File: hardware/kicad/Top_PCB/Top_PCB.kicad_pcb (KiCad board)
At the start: 2 copper layers, 30.8 x 26.8 mm, 3 parts, among them J1 XT30PW-M

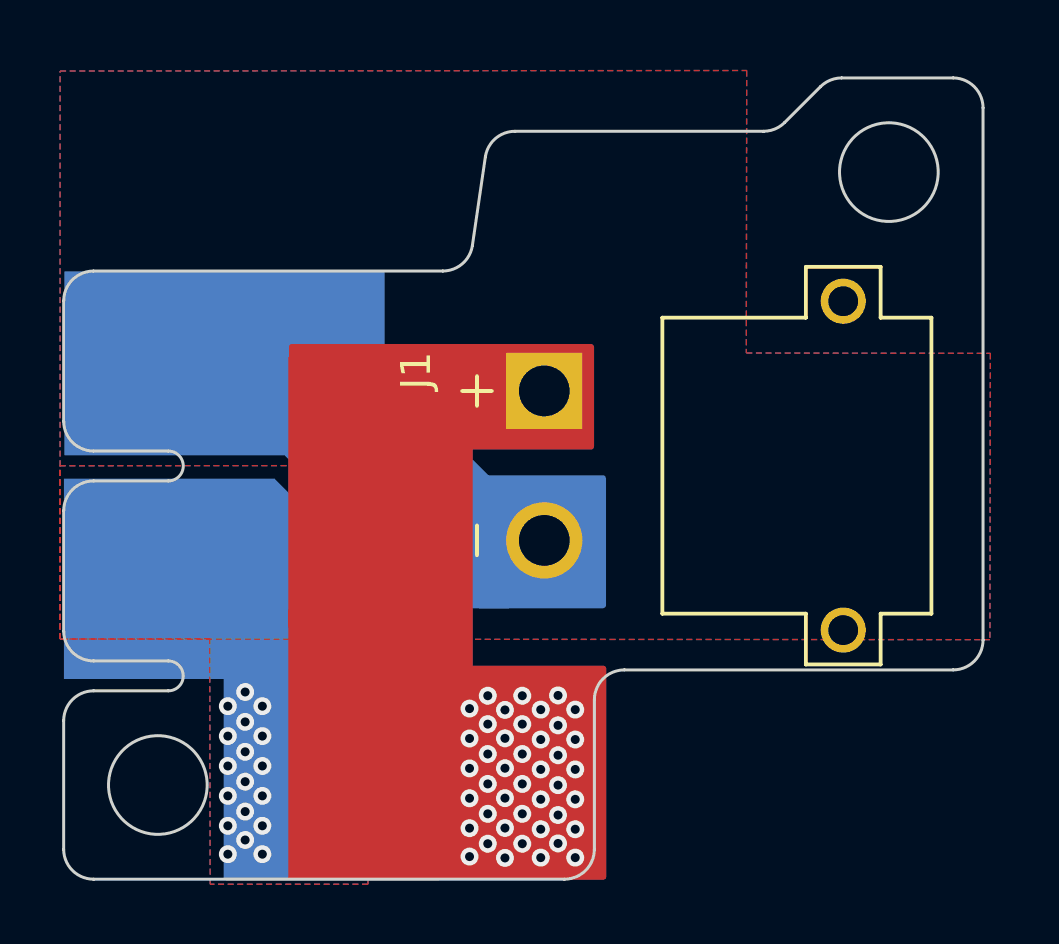
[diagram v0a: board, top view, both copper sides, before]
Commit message: Did some top board work (added regulator), added vias and refined geometry a bit
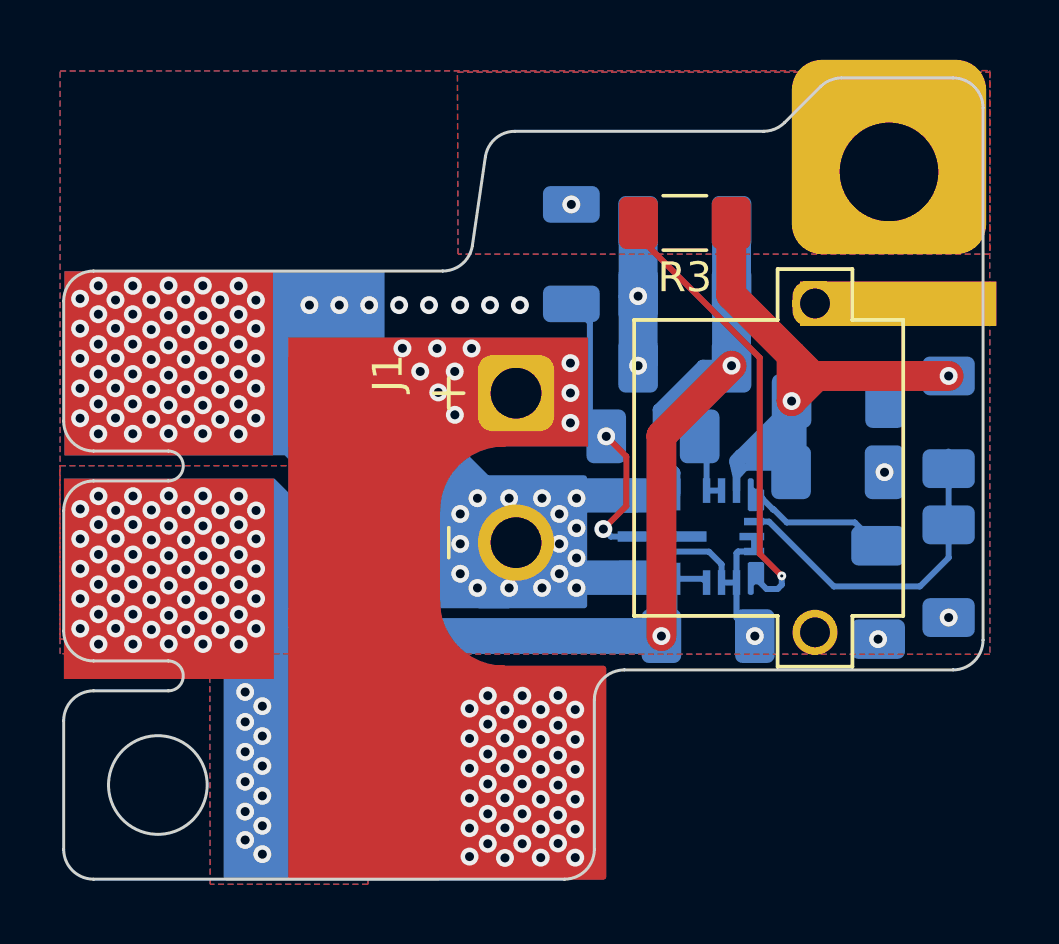
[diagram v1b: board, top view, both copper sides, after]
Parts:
- added C2: 10uF, Capacitor_SMD:C_1206_3216Metric_Pad1.33x1.80mm_HandSolder, B.Cu at (131.5, 89.3)
- added C3: 10uF, Capacitor_SMD:C_1206_3216Metric_Pad1.33x1.80mm_HandSolder, B.Cu at (131.5, 91.7)
- added C4: 1uF, Capacitor_SMD:C_1206_3216Metric_Pad1.33x1.80mm_HandSolder, B.Cu at (131.5, 94.1)
- added C5: 1uF, Capacitor_SMD:C_1206_3216Metric_Pad1.33x1.80mm_HandSolder, B.Cu at (132.3, 103.1)
- added C6: 100nF, Capacitor_SMD:C_1206_3216Metric_Pad1.33x1.80mm_HandSolder, B.Cu at (130.4, 96.4)
- added C7: 22uF, Capacitor_SMD:C_1206_3216Metric_Pad1.33x1.80mm_HandSolder, B.Cu at (136.6, 95.2)
- added C8: 1uF, Capacitor_SMD:C_1206_3216Metric_Pad1.33x1.80mm_HandSolder, B.Cu at (138.0, 101.6)
- added C9: 100nF, Capacitor_SMD:C_1206_3216Metric_Pad1.33x1.80mm_HandSolder, B.Cu at (136.6, 97.6)
- added L1: 640nH, Inductor_SMD:L_1206_3216Metric_Pad1.22x1.90mm_HandSolder, B.Cu at (127.7, 90.3)
- added R1: 100k, PCB-V2-Footprints:R_1206_3216Metric_Pad1.30x1.75mm_HandSolder, B.Cu at (140.3, 96.0)
- added R2: 14.3k, PCB-V2-Footprints:R_1206_3216Metric_Pad1.30x1.75mm_HandSolder, B.Cu at (140.3, 100.9)
- added R3: 100k, PCB-V2-Footprints:R_1206_3216Metric_Pad1.30x1.75mm_HandSolder, F.Cu at (131.5, 89.3)
- added U1: LM61495RPHR, LM61480Q3RPHRQ1:RPH0016A, B.Cu at (131.7, 99.8)
- added VCC_8V1: ~, Pads:VCC_Standalone, B.Cu at (138.3, 87.6)
- moved J1 0.95 mm to (135.8, 97.5)
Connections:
- J1 pad S1: (no net) -> GND
- J1 pad S2: (no net) -> GND
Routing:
- net VCC_4S: track 0.00 -> 36.8 mm, vias 18 -> 74
- net Net-(U1-BIAS): track 0.00 -> 25.8 mm, vias 0 -> 3
- net GND: track 0.00 -> 20.3 mm, vias 0 -> 90
- net Net-(U1-RESET): track 0.00 -> 15.2 mm, vias 0 -> 1
- net Net-(U1-FB): track 0.00 -> 10.8 mm
- net Net-(U1-SW): track 0.00 -> 10.7 mm, vias 0 -> 2
- net Net-(U1-VCC): track 0.00 -> 4.82 mm
- net Net-(U1-CBOOT): track 0.00 -> 2.41 mm
- net Net-(Fingertech_Switch1-PadIN): vias 42 -> 52
- added copper zone on B.Cu, net Net-(U1-BIAS)
- added copper zone on F.Cu, net Net-(U1-BIAS)
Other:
- outline, holes or cut-outs redrawn

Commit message: Bottom PCB Design Checked and should be ready for review
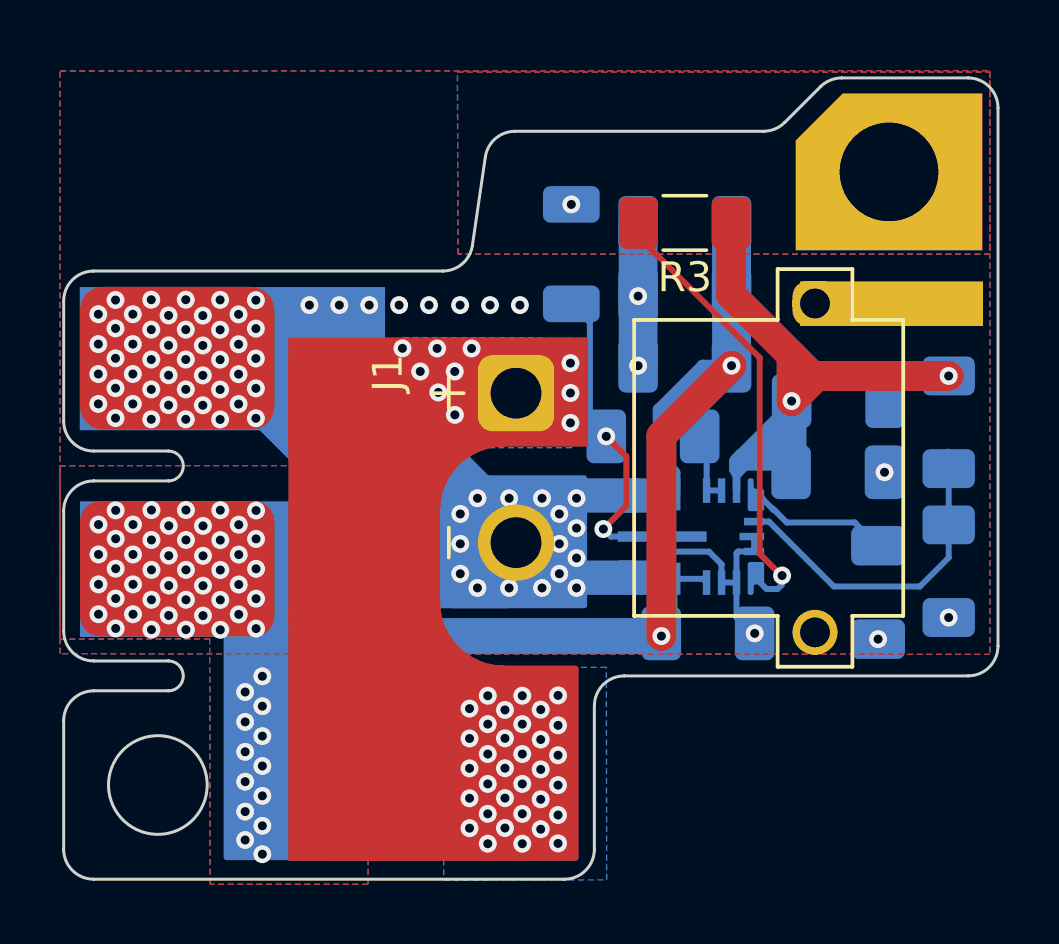
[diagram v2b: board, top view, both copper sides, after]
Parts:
- moved C5 0.09 mm to (132.3, 103.0)
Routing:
- net Net-(U1-BIAS): track 25.8 -> 22.7 mm
- net GND: vias 90 -> 75
- net VCC_4S: vias 74 -> 60
- net Net-(Fingertech_Switch1-PadIN): vias 52 -> 43
- added copper zone on B.Cu, net Net-(Fingertech_Switch1-PadIN)
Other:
- board size 30.8 x 26.8 mm -> 31.2 x 26.8 mm
